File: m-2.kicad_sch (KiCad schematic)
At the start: 50 parts, among them J301 1-2199230-6, J302 1-2199230-6, M301 M2_2280, M302 M2_2280, P301 2199230-6, U301 74LVC2G07GV,125, U302 74LVC2G07GV,125

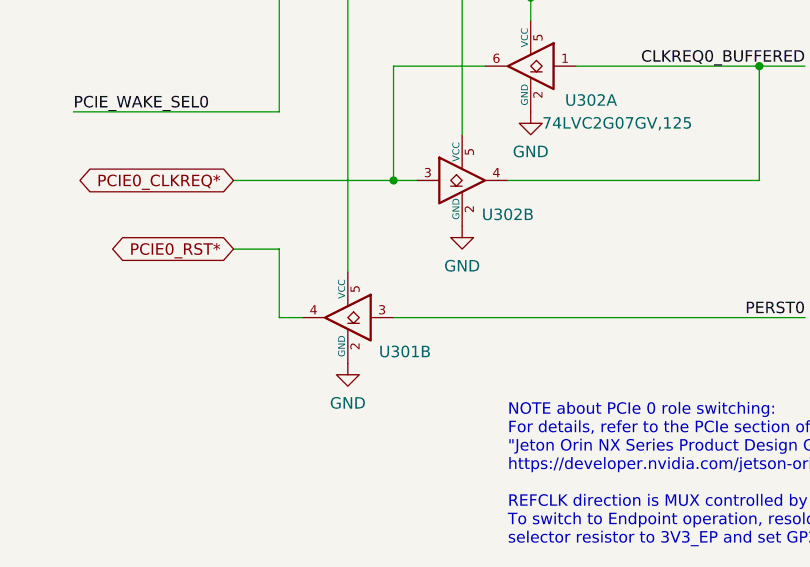
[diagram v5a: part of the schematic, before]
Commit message: Fix mixed U302, U301 connections
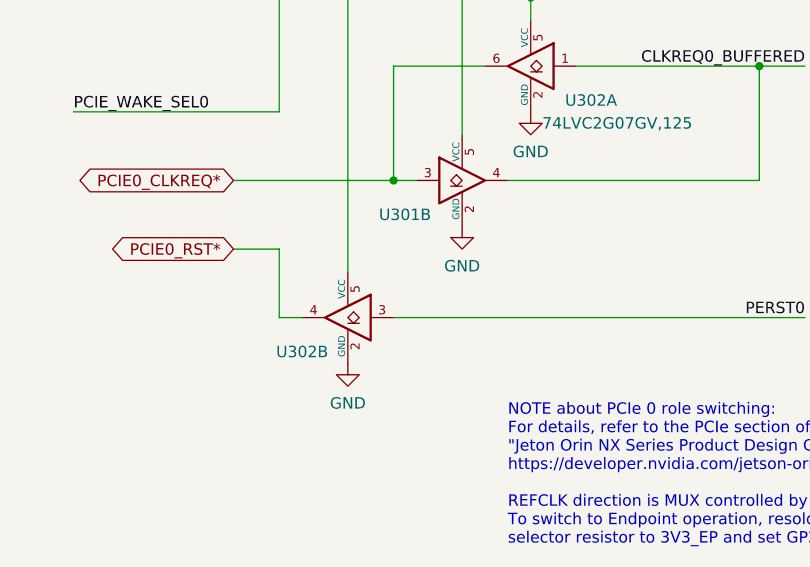
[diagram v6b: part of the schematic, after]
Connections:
- net 3V3_EP: now also U302.5 (VCC); no longer U301.5 (VCC)
- net 3V3_RP: now also U301.5 (VCC); no longer U302.5 (VCC)
- net CLKREQ0_BUFFERED: now also U301.4; no longer U302.4
- net PCIE0_CLKREQ*: now also U301.3; no longer U302.3
- net PCIE0_RST*: now also U302.4; no longer U301.4
- net PERST0: now also U302.3; no longer U301.3
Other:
- moved on the sheet: U301B, U302B
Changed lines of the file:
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@@
     (pin "1")
   )
-  (symbol (lib_id "antmicroLogicBuffersDriversReceiversTransceivers:74LVC2G07GV,125") (at 190.5 236.22 0) (unit 2)
-    (in_bom yes) (on_board yes)
-    (property "Reference" "U302" (id 0) (at 195.58 240.03 0))
-    (property "Value" "74LVC2G07GV,125" (id 1) (at 193.04 241.3 0)
+  (symbol (lib_id "antmicroLogicBuffersDriversReceiversTransceivers:74LVC2G07GV,125") (at 177.8 251.46 0) (mirror y) (unit 2)
+    (in_bom yes) (on_board yes)
+    (property "Reference" "U302" (id 0) (at 172.72 255.27 0))
+    (property "Value" "74LVC2G07GV,125" (id 1) (at 175.26 256.54 0)
       (effects (font (size 1.27 1.27)) (justify left) hide)
     )
-    (property "Footprint" "antmicro-footprints:SC-74" (id 2) (at 205.486 243.84 0)
-      (effects (font (size 1.27 1.27)) hide)
-    )
-    (property "Datasheet" "https://www.tme.eu/Document/2ad9356043a4952b9021ef50162f8c34/74LVC2G07.pdf" (id 3) (at 192.405 248.92 0)
+    (property "Footprint" "antmicro-footprints:SC-74" (id 2) (at 162.814 259.08 0)
+      (effects (font (size 1.27 1.27)) hide)
+    )
+    (property "Datasheet" "https://www.tme.eu/Document/2ad9356043a4952b9021ef50162f8c34/74LVC2G07.pdf" (id 3) (at 175.895 264.16 0)
       (effects (font (size 1.27 1.27)) (justify left) hide)
     )
-    (property "Manufacturer" "Nexperia" (id 4) (at 196.596 246.38 0)
-      (effects (font (size 1.27 1.27)) hide)
-    )
-    (property "MPN" "74LVC2G07GV,125" (id 5) (at 209.931 246.38 0)
+    (property "Manufacturer" "Nexperia" (id 4) (at 171.704 261.62 0)
+      (effects (font (size 1.27 1.27)) hide)
+    )
+    (property "MPN" "74LVC2G07GV,125" (id 5) (at 158.369 261.62 0)
       (effects (font (size 1.27 1.27)) hide)
     )
@@
     (pin "2")
   )
-  (symbol (lib_id "antmicroLogicBuffersDriversReceiversTransceivers:74LVC2G07GV,125") (at 177.8 251.46 0) (mirror y) (unit 2)
-    (in_bom yes) (on_board yes)
-    (property "Reference" "U301" (id 0) (at 184.15 255.27 0))
-    (property "Value" "74LVC2G07GV,125" (id 1) (at 190.5 250.1392 0)
-      (effects (font (size 1.27 1.27)) hide)
-    )
-    (property "Footprint" "antmicro-footprints:SC-74" (id 2) (at 162.814 259.08 0)
-      (effects (font (size 1.27 1.27)) hide)
-    )
-    (property "Datasheet" "https://www.tme.eu/Document/2ad9356043a4952b9021ef50162f8c34/74LVC2G07.pdf" (id 3) (at 175.895 264.16 0)
+  (symbol (lib_id "antmicroLogicBuffersDriversReceiversTransceivers:74LVC2G07GV,125") (at 190.5 236.22 0) (unit 2)
+    (in_bom yes) (on_board yes)
+    (property "Reference" "U301" (id 0) (at 184.15 240.03 0))
+    (property "Value" "74LVC2G07GV,125" (id 1) (at 177.8 234.8992 0)
+      (effects (font (size 1.27 1.27)) hide)
+    )
+    (property "Footprint" "antmicro-footprints:SC-74" (id 2) (at 205.486 243.84 0)
+      (effects (font (size 1.27 1.27)) hide)
+    )
+    (property "Datasheet" "https://www.tme.eu/Document/2ad9356043a4952b9021ef50162f8c34/74LVC2G07.pdf" (id 3) (at 192.405 248.92 0)
       (effects (font (size 1.27 1.27)) (justify left) hide)
     )
-    (property "Manufacturer" "Nexperia" (id 4) (at 171.704 261.62 0)
-      (effects (font (size 1.27 1.27)) hide)
-    )
-    (property "MPN" "74LVC2G07GV,125" (id 5) (at 158.369 261.62 0)
-      (effects (font (size 1.27 1.27)) hide)
-    )
+    (property "Manufacturer" "Nexperia" (id 4) (at 196.596 246.38 0)
+      (effects (font (size 1.27 1.27)) hide)
+    )
+    (property "MPN" "74LVC2G07GV,125" (id 5) (at 209.931 246.38 0)
+      (effects (font (size 1.27 1.27)) hide)
+    )

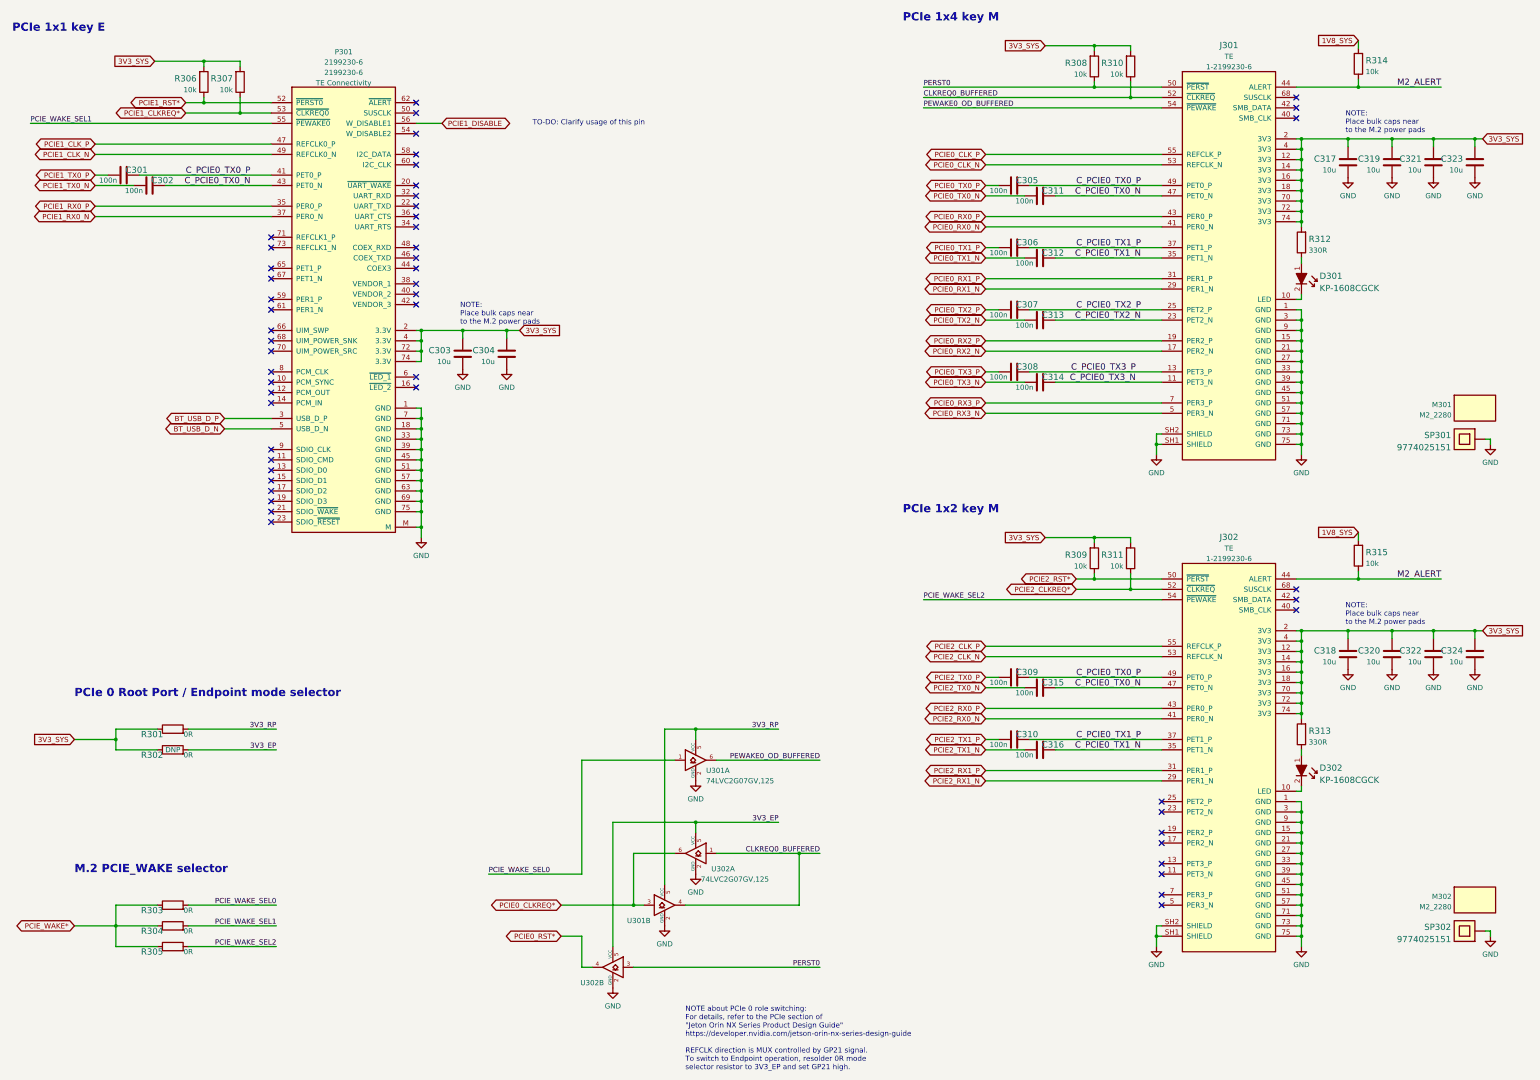
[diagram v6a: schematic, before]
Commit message: Cleaned up the schematic, fixed library issues, annotated schematic
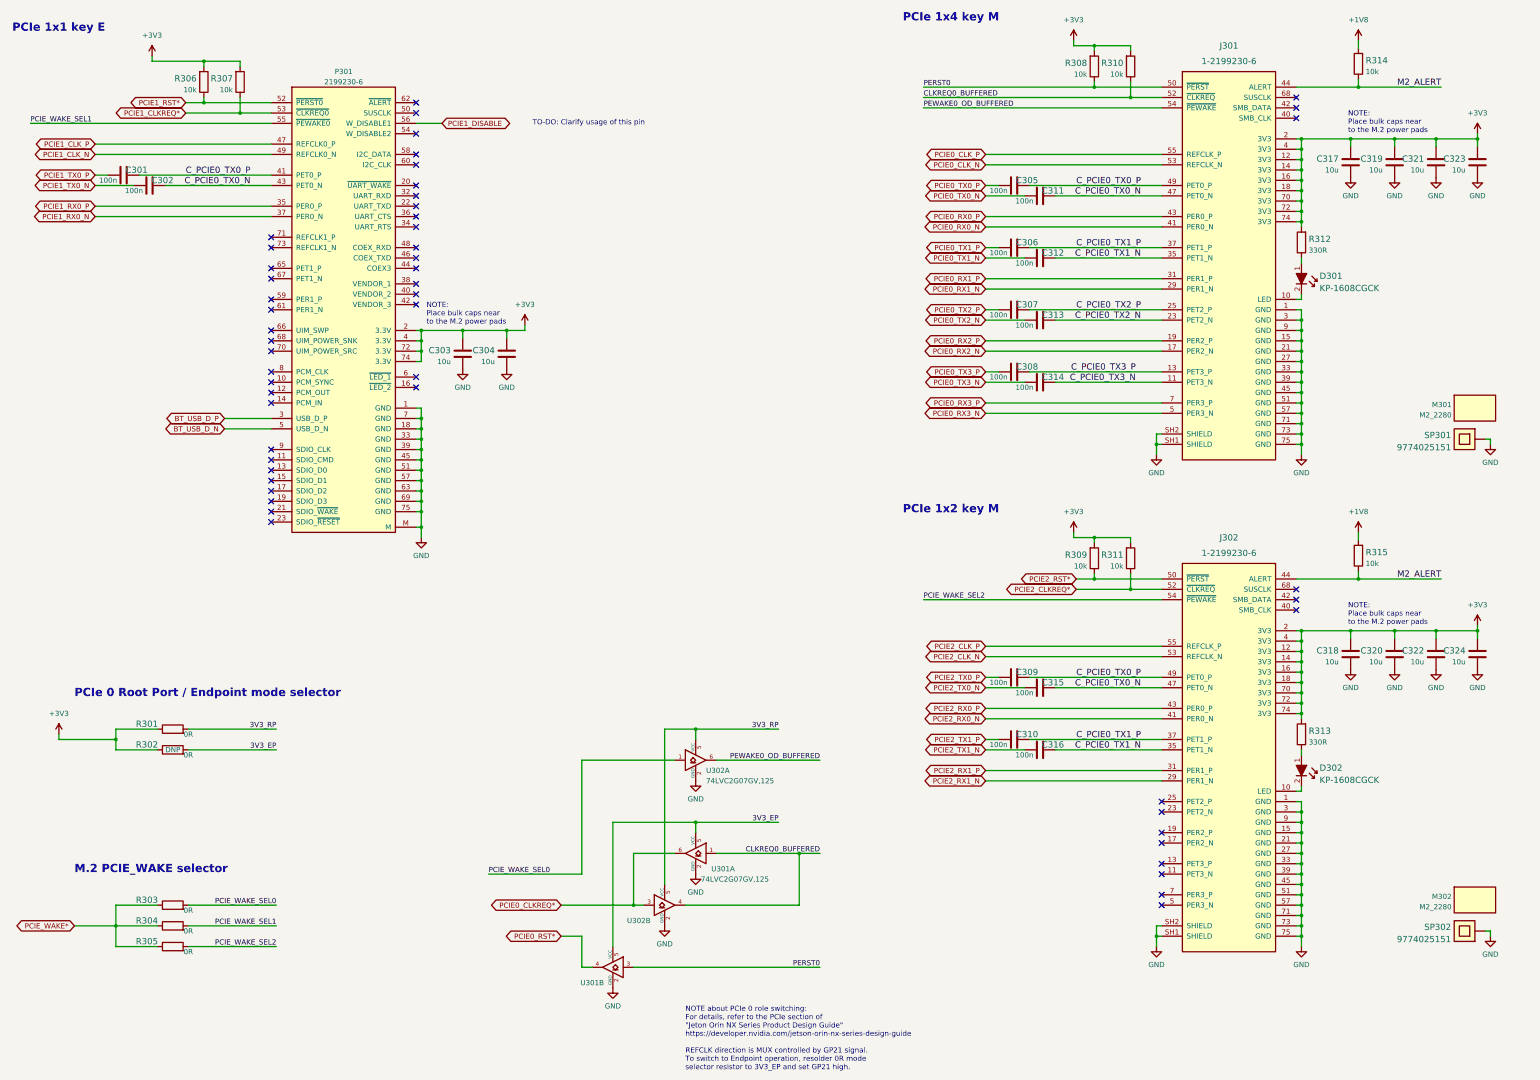
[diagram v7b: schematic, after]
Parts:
- renumbered U302 to U301, U301 to U302
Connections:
- net 1V8_SYS renamed +1V8
- net 3V3_SYS renamed +3V3
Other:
- moved on the sheet: C318, C320, C322, C324

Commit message: Unified schematic look of ethernet sheet, improved shielding of eth connector, replaced gnd symbols
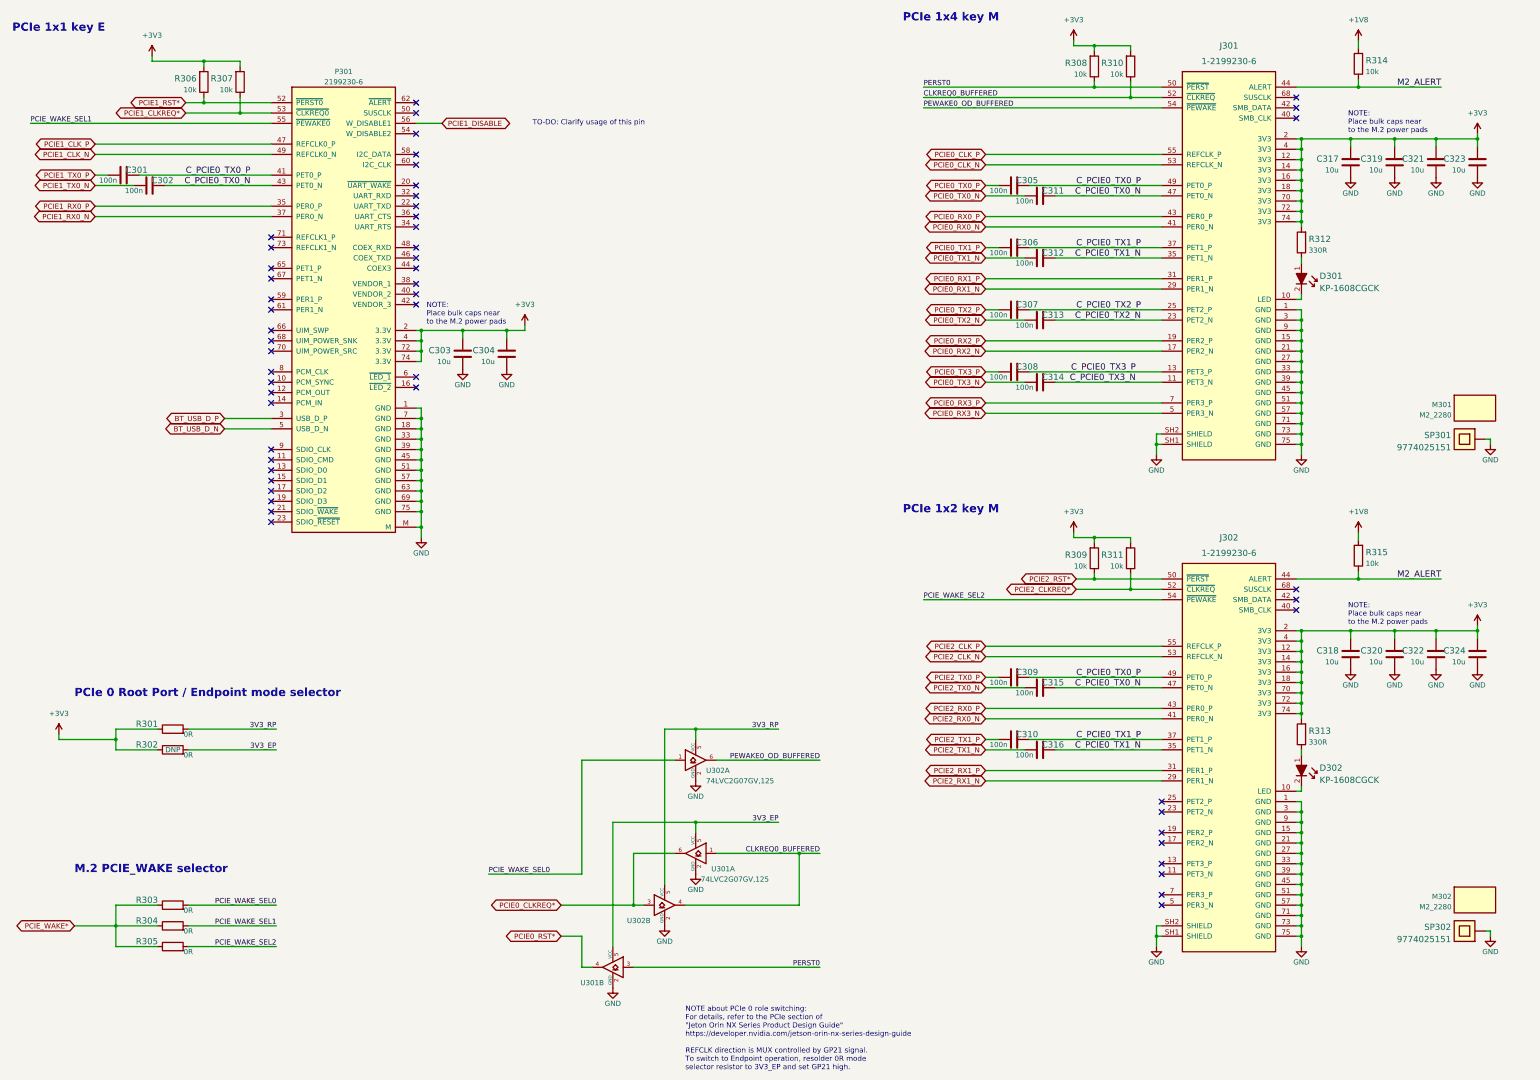
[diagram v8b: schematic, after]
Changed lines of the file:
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@@
       (effects (font (size 1.27 1.27)) hide)
     )
-    (property "Value" "GND" (id 1) (at 151.765 109.2184 0))
+    (property "Value" "GND" (id 1) (at 151.765 108.585 0))
     (property "Footprint" "" (id 2) (at 151.765 104.775 0)
       (effects (font (size 1.27 1.27)) hide)
@@
       (effects (font (size 1.27 1.27)) hide)
     )
-    (property "Value" "GND" (id 1) (at 369.57 182.8784 0))
+    (property "Value" "GND" (id 1) (at 369.57 182.245 0))
     (property "Footprint" "" (id 2) (at 369.57 178.435 0)
       (effects (font (size 1.27 1.27)) hide)
@@
       (effects (font (size 1.27 1.27)) hide)
     )
-    (property "Value" "GND" (id 1) (at 177.8 260.9834 0))
+    (property "Value" "GND" (id 1) (at 177.8 260.35 0))
     (property "Footprint" "" (id 2) (at 177.8 256.54 0)
       (effects (font (size 1.27 1.27)) hide)
@@
       (effects (font (size 1.27 1.27)) hide)
     )
-    (property "Value" "GND" (id 1) (at 311.15 130.1734 0))
+    (property "Value" "GND" (id 1) (at 311.15 129.54 0))
     (property "Footprint" "" (id 2) (at 311.15 125.73 0)
       (effects (font (size 1.27 1.27)) hide)
@@
       (effects (font (size 1.27 1.27)) hide)
     )
-    (property "Value" "GND" (id 1) (at 389.89 182.8784 0))
+    (property "Value" "GND" (id 1) (at 389.89 182.245 0))
     (property "Footprint" "" (id 2) (at 389.89 178.435 0)
       (effects (font (size 1.27 1.27)) hide)
@@
       (effects (font (size 1.27 1.27)) hide)
     )
-    (property "Value" "GND" (id 1) (at 379.73 182.8784 0))
+    (property "Value" "GND" (id 1) (at 379.73 182.245 0))
     (property "Footprint" "" (id 2) (at 379.73 178.435 0)
       (effects (font (size 1.27 1.27)) hide)
@@
       (effects (font (size 1.27 1.27)) hide)
     )
-    (property "Value" "GND" (id 1) (at 190.5 245.7434 0))
+    (property "Value" "GND" (id 1) (at 190.5 245.11 0))
     (property "Footprint" "" (id 2) (at 190.5 241.3 0)
       (effects (font (size 1.27 1.27)) hide)
@@
       (effects (font (size 1.27 1.27)) hide)
     )
-    (property "Value" "GND" (id 1) (at 346.71 130.1734 0))
+    (property "Value" "GND" (id 1) (at 346.71 129.54 0))
     (property "Footprint" "" (id 2) (at 346.71 125.73 0)
       (effects (font (size 1.27 1.27)) hide)
@@
       (effects (font (size 1.27 1.27)) hide)
     )
-    (property "Value" "GND" (id 1) (at 379.73 62.2284 0))
+    (property "Value" "GND" (id 1) (at 379.73 61.595 0))
     (property "Footprint" "" (id 2) (at 379.73 57.785 0)
       (effects (font (size 1.27 1.27)) hide)
@@
       (effects (font (size 1.27 1.27)) hide)
     )
-    (property "Value" "GND" (id 1) (at 140.97 109.2184 0))
+    (property "Value" "GND" (id 1) (at 140.97 108.585 0))
     (property "Footprint" "" (id 2) (at 140.97 104.775 0)
       (effects (font (size 1.27 1.27)) hide)
@@
       (effects (font (size 1.27 1.27)) hide)
     )
-    (property "Value" "GND" (id 1) (at 130.81 150.4934 0))
+    (property "Value" "GND" (id 1) (at 130.81 149.86 0))
     (property "Footprint" "" (id 2) (at 130.81 146.05 0)
       (effects (font (size 1.27 1.27)) hide)
@@
       (effects (font (size 1.27 1.27)) hide)
     )
-    (property "Value" "GND" (id 1) (at 358.775 182.8784 0))
+    (property "Value" "GND" (id 1) (at 358.775 182.245 0))
     (property "Footprint" "" (id 2) (at 358.775 178.435 0)
       (effects (font (size 1.27 1.27)) hide)
@@
       (effects (font (size 1.27 1.27)) hide)
     )
-    (property "Value" "GND" (id 1) (at 198.12 210.1834 0))
+    (property "Value" "GND" (id 1) (at 198.12 209.55 0))
     (property "Footprint" "" (id 2) (at 198.12 205.74 0)
       (effects (font (size 1.27 1.27)) hide)
@@
       (effects (font (size 1.27 1.27)) hide)
     )
-    (property "Value" "GND" (id 1) (at 369.57 62.2284 0))
+    (property "Value" "GND" (id 1) (at 369.57 61.595 0))
     (property "Footprint" "" (id 2) (at 369.57 57.785 0)
       (effects (font (size 1.27 1.27)) hide)
@@
       (effects (font (size 1.27 1.27)) hide)
     )
-    (property "Value" "GND" (id 1) (at 346.71 250.8234 0))
+    (property "Value" "GND" (id 1) (at 346.71 250.19 0))
     (property "Footprint" "" (id 2) (at 346.71 246.38 0)
       (effects (font (size 1.27 1.27)) hide)
@@
       (effects (font (size 1.27 1.27)) hide)
     )
-    (property "Value" "GND" (id 1) (at 198.12 233.0434 0))
+    (property "Value" "GND" (id 1) (at 198.12 232.41 0))
     (property "Footprint" "" (id 2) (at 198.12 228.6 0)
       (effects (font (size 1.27 1.27)) hide)
@@
       (effects (font (size 1.27 1.27)) hide)
     )
-    (property "Value" "GND" (id 1) (at 393.065 248.2834 0))
+    (property "Value" "GND" (id 1) (at 393.065 247.65 0))
     (property "Footprint" "" (id 2) (at 393.065 243.84 0)
       (effects (font (size 1.27 1.27)) hide)
@@
       (effects (font (size 1.27 1.27)) hide)
     )
-    (property "Value" "GND" (id 1) (at 389.89 62.2284 0))
+    (property "Value" "GND" (id 1) (at 389.89 61.595 0))
     (property "Footprint" "" (id 2) (at 389.89 57.785 0)
       (effects (font (size 1.27 1.27)) hide)
@@
       (effects (font (size 1.27 1.27)) hide)
     )
-    (property "Value" "GND" (id 1) (at 358.775 62.2284 0))
+    (property "Value" "GND" (id 1) (at 358.775 61.595 0))
     (property "Footprint" "" (id 2) (at 358.775 57.785 0)
       (effects (font (size 1.27 1.27)) hide)
@@
       (effects (font (size 1.27 1.27)) hide)
     )
-    (property "Value" "GND" (id 1) (at 311.15 250.8234 0))
+    (property "Value" "GND" (id 1) (at 311.15 250.19 0))
     (property "Footprint" "" (id 2) (at 311.15 246.38 0)
       (effects (font (size 1.27 1.27)) hide)
@@
       (effects (font (size 1.27 1.27)) hide)
     )
-    (property "Value" "GND" (id 1) (at 393.065 127.6334 0))
+    (property "Value" "GND" (id 1) (at 393.065 127 0))
     (property "Footprint" "" (id 2) (at 393.065 123.19 0)
       (effects (font (size 1.27 1.27)) hide)
